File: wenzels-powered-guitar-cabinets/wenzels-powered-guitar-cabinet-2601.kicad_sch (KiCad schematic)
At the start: 64 parts, among them J1 AC power in, J10 IN 2, J11 IN 3, J12 IN 4, J2 2-channel TPA3255 Class D amp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, J3 Speaker Out 2, J4 Switching-Mode Power Supply, J5 2-channel TPA3255 Class D amp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, J6 Speaker Out 3, J7 Speaker Out 4, J8 IN 1, J9 Speaker Out 1, M1 12V Noctua NF-A9 PWM 92mm, M2 12V Noctua NF-A9 PWM 92mm, M3 12V Noctua NF-A9 PWM 92mm, T1 TY250P, T2 TY250P, T3 TY250P, T4 TY250P

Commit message: wenzels-powered-guitar-cabinets release-2601-cabinet-2026-02-r2
Fixed ground loop switching power supply noise by introducing series 10Ω
resistor for the input grounds.
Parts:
- added R10, R11, R12, R13: 10, symbol Device:R
- added SW1: GND-1, symbol Switch:SW_SPDT_MSM
- added SW2: GND-2, symbol Switch:SW_SPDT_MSM
- added SW3, SW4: GND-3, symbol Switch:SW_SPDT_MSM
- PS1: Field14 (none) -> At ≈6V these Noctua fans are barely audible.
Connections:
- net Ports panel shield: now also SW1.2 (3); no longer J10.S, J10.SN, J11.S, J11.SN, J12.S, J12.SN, J2.3 (Pin_3), J5.3 (Pin_3), T1.3 (IN-), T2.3 (IN-), T3.3 (IN-), T4.3 (IN-)
- new net: J11.S, J11.SN, SW3.2 (3)
- new net: J12.S, J12.SN, SW4.2 (3)
- new net: J10.S, J10.SN, SW2.2 (3)
- new net 2: J2.3 (Pin_3), J5.3 (Pin_3), R10.2, R11.2, R12.2, R13.2, SW1.3 (4), SW2.3 (4), SW3.3 (4), SW4.3 (4), T1.3 (IN-), T2.3 (IN-), T3.3 (IN-), T4.3 (IN-)
- new net R-Lifted : R10.1, R11.1, R12.1, R13.1, SW1.1, SW2.1, SW3.1, SW4.1
- no-connect marks 5 -> 9
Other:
- note added: "Ground-lifting switches. Ground-lifting is important in my setup. If I connect the ground I get the switching high-pitch noise (probably coming from the power supply). If I disconnect it completely I get loud buzz/hum (even though my signal has its own path to ground before it hits the amps), sounds like 60Hz wall power hum, but very loud. Only when I lift the ground with a 10Ω resistor it gets s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"
- note added: "In my build the DF reduction resistors are actually distributed between 2 heatsinks for each amplifier (not like on this schematic). 1st channel positive goes through 1st resistor on 1st heat sink, and negative goes through 1st resistor on the 2nd heatsink. And so on. It doesn’t really matter, I just did it this way because it was easier for the wires to reach the resistors. But this might be a b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"

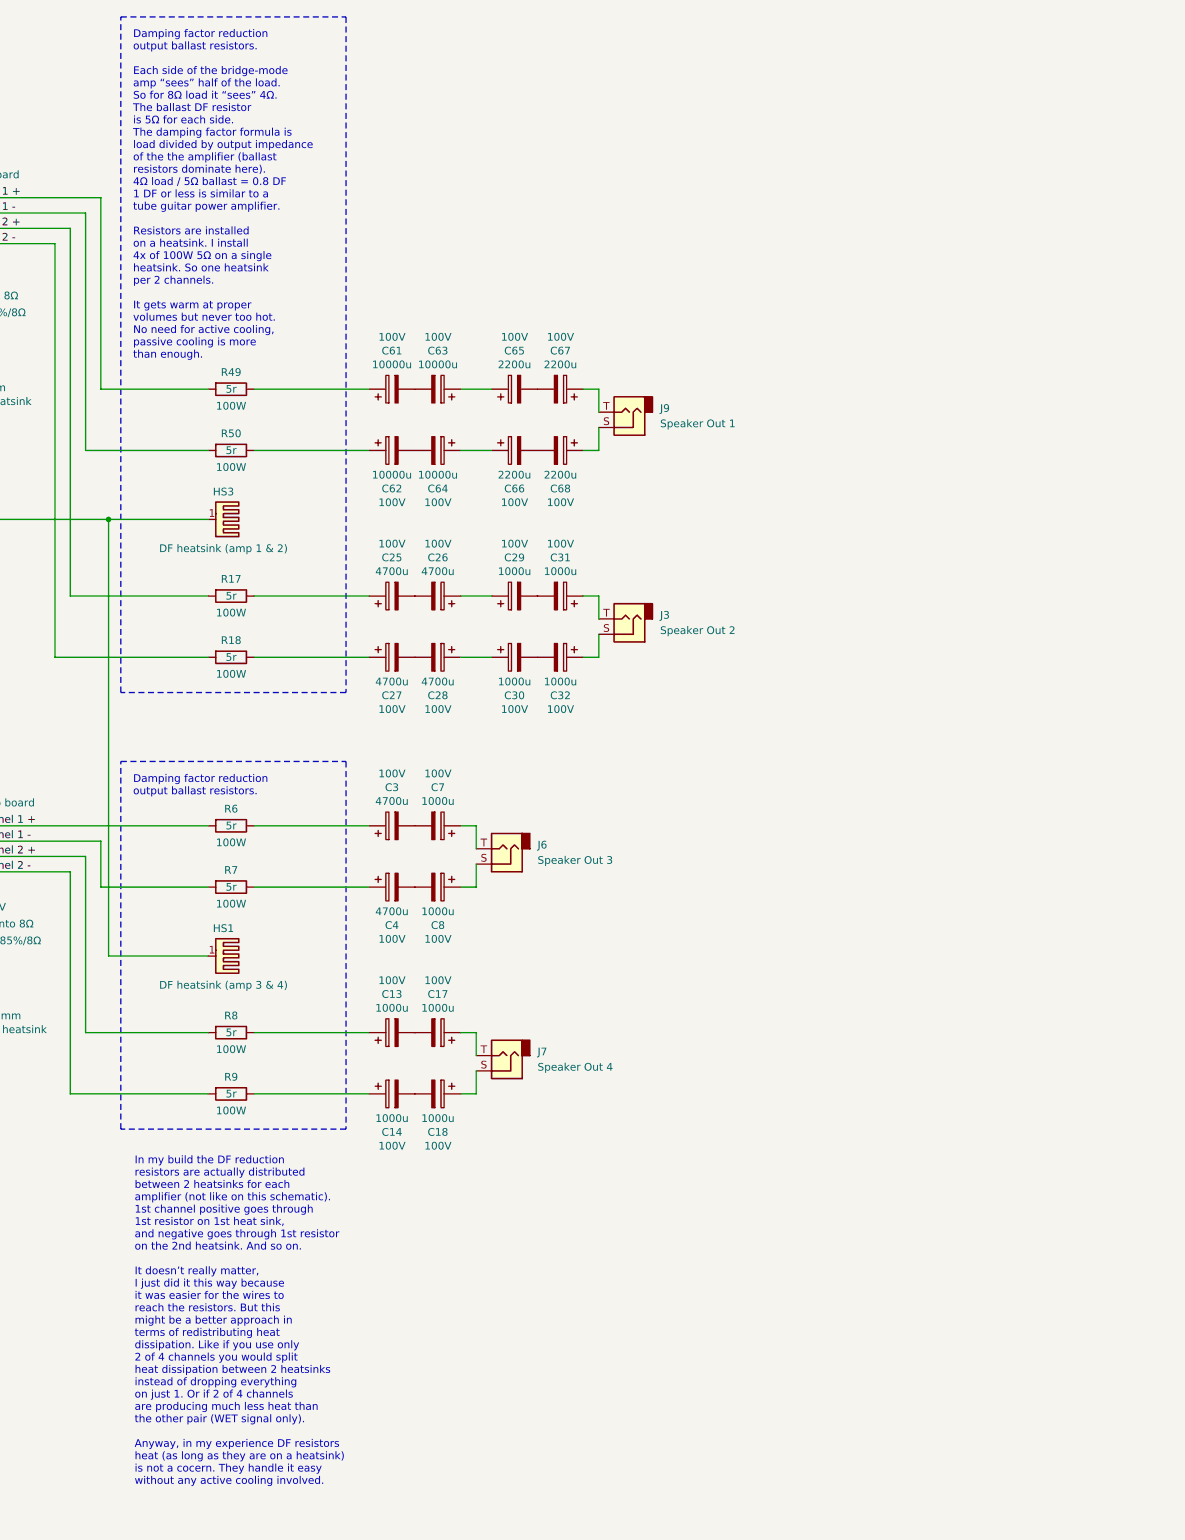
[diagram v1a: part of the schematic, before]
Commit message: wenzels-powered-guitar-cabinets 2601-r3 & 2602-r2 releases
Added impedance transformers and bleeder resistors for the output
capacitors.
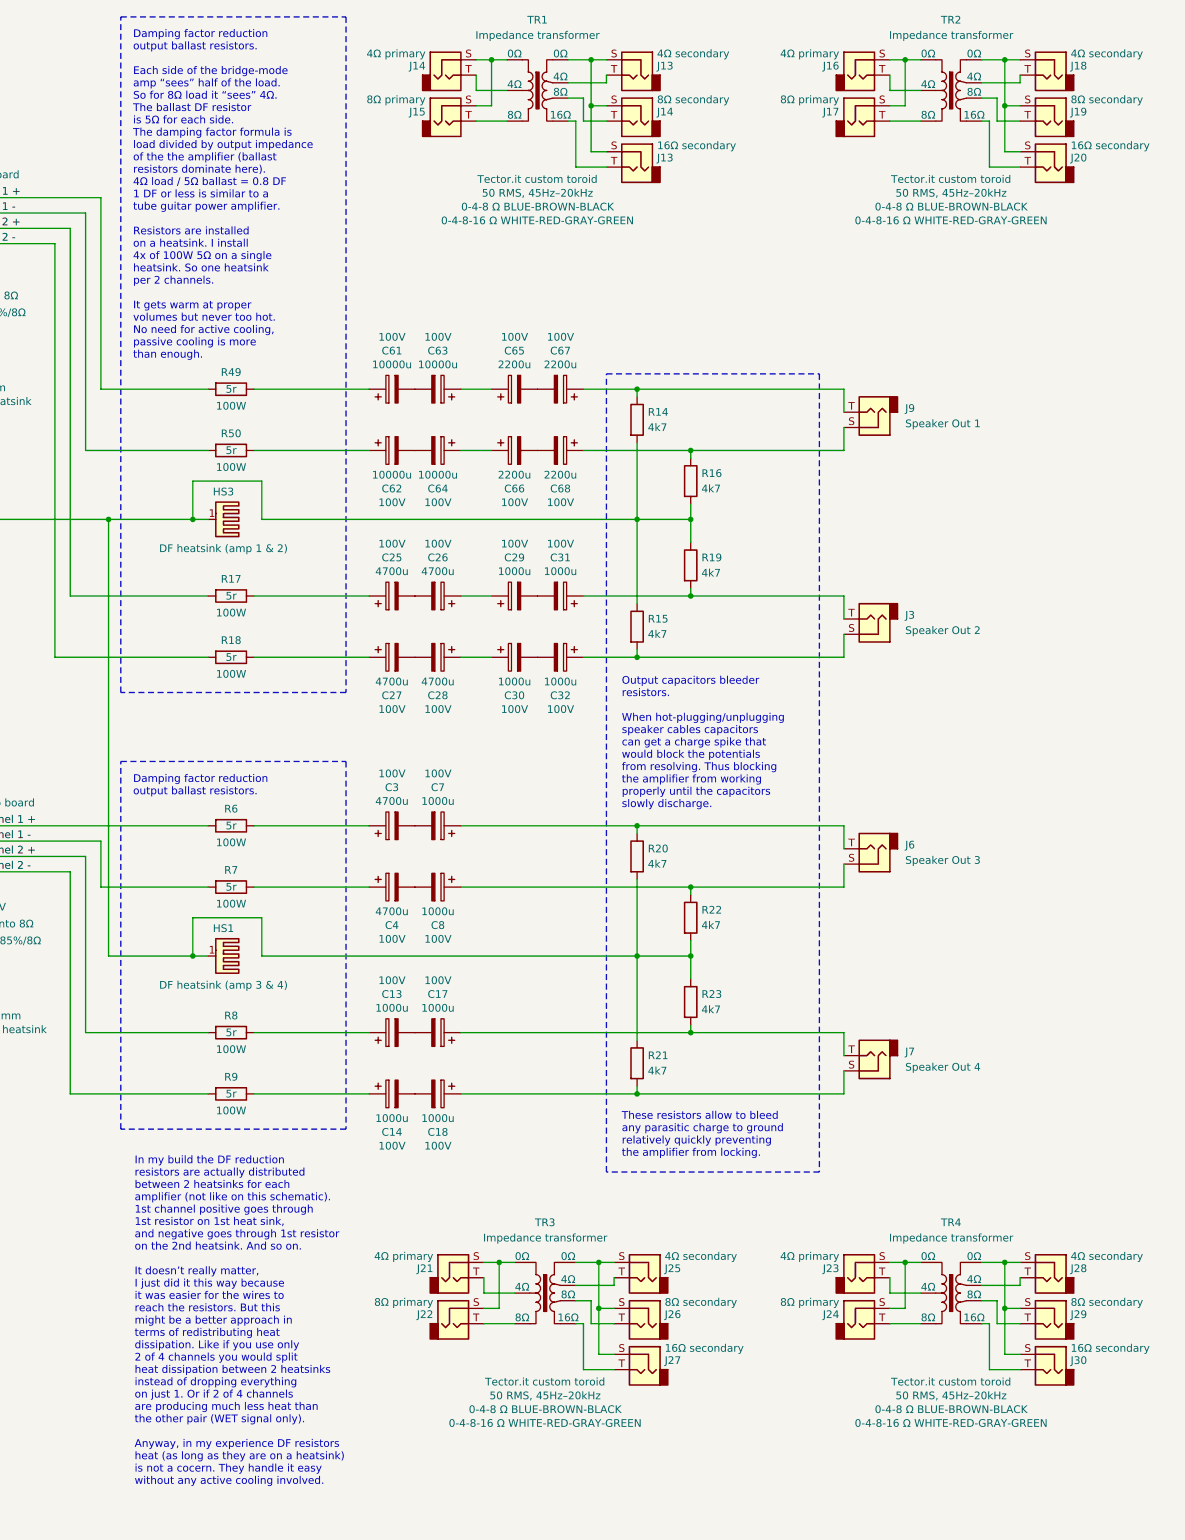
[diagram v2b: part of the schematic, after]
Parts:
- added J13, J18, J25, J28: 4Ω secondary, symbol Connector_Audio:AudioJack2
- added J13, J20, J27, J30: 16Ω secondary, symbol Connector_Audio:AudioJack2
- added J14, J16, J21, J23: 4Ω primary, symbol Connector_Audio:AudioJack2
- added J14, J19, J26, J29: 8Ω secondary, symbol Connector_Audio:AudioJack2
- added J15, J17, J22, J24: 8Ω primary, symbol Connector_Audio:AudioJack2
- added R14, R15, R16, R19, R20, R21, R22, R23: 4k7, symbol Device:R
- added TR1, TR2, TR3, TR4: Impedance transformer, symbol Transformer:TRANSF4
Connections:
- net -24V: now also R14.2, R15.1, R16.2, R19.1, R20.2, R21.1, R22.2, R23.1
- net at C67.1, J9.T: now also R14.1
- net at C18.1, J7.S: now also R21.2
- net at C32.1, J3.S: now also R15.2
- net at C31.1, J3.T: now also R19.2
- net at C8.1, J6.S: now also R22.1
- net at C68.1, J9.S: now also R16.1
- net at C17.1, J7.T: now also R23.2
- net at C7.1, J6.T: now also R20.1
- new net: J18.S, J19.S, J20.S, TR2.4 (0Ω)
- new net: J19.T, TR2.6 (8Ω)
- new net: J25.S, J26.S, J27.S, TR3.4 (0Ω)
- new net: J25.T, TR3.5 (4Ω)
- new net: J14.S, J15.S, TR1.1 (0Ω)
- new net: J15.T, TR1.3 (8Ω)
- new net: J21.S, J22.S, TR3.1 (0Ω)
- new net: J21.T, TR3.2 (4Ω)
- new net: J22.T, TR3.3 (8Ω)
- new net: J26.T, TR3.6 (8Ω)
- new net: J27.T, TR3.7 (16Ω)
- new net: J14.T, TR1.2 (4Ω)
- new net: J13.S, J13.S, J14.S, TR1.4 (0Ω)
- new net: J13.T, TR1.5 (4Ω)
- new net: J28.S, J29.S, J30.S, TR4.4 (0Ω)
- new net: J28.T, TR4.5 (4Ω)
- new net: J23.S, J24.S, TR4.1 (0Ω)
- new net: J24.T, TR4.3 (8Ω)
- new net: J16.S, J17.S, TR2.1 (0Ω)
- new net: J16.T, TR2.2 (4Ω)
- new net: J17.T, TR2.3 (8Ω)
- new net: J18.T, TR2.5 (4Ω)
- new net: J20.T, TR2.7 (16Ω)
- new net: J23.T, TR4.2 (4Ω)
- new net: J29.T, TR4.6 (8Ω)
- new net: J30.T, TR4.7 (16Ω)
- new net: J14.T, TR1.6 (8Ω)
- new net: J13.T, TR1.7 (16Ω)
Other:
- note added: "Output capacitors bleeder resistors. When hot-plugging/unplugging speaker cables capacitors can get a charge spike that would block the potentials from resolving. Thus blocking the amplifier from working properly until the capacitors slowly discharge."
- note added: "These resistors allow to bleed any parasitic charge to ground relatively quickly preventing the amplifier from locking."
- moved on the sheet: J3, J6, J7, J9
